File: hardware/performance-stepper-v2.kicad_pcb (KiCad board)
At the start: 4 copper layers, 80 x 80 mm, 111 parts, among them P1 VIN, P101 CON-SENSOR2, P102 DEBUG, P103 BOOT, P2 OUT, P3 GPIO, P4 PROTO, Q1 CSD19533Q5A, Q2 CSD19533Q5A, Q3 CSD19533Q5A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

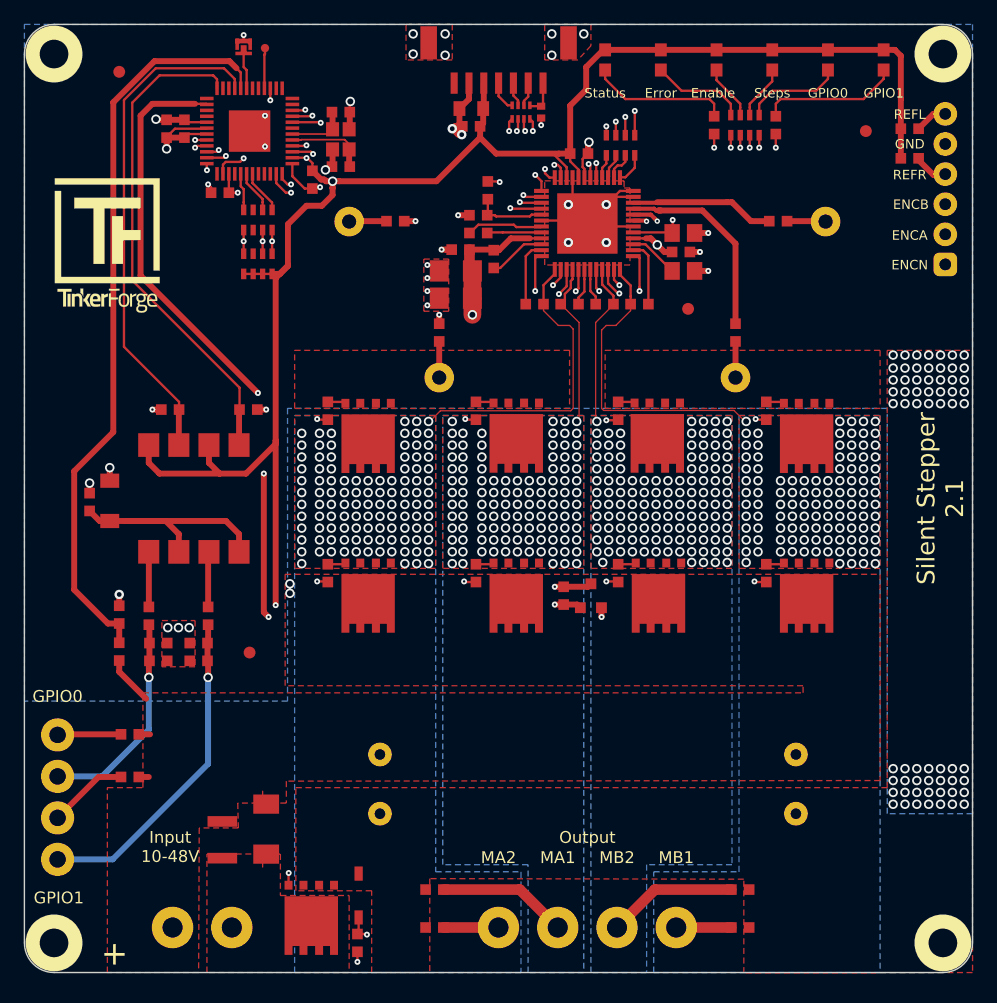
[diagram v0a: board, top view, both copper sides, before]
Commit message: version 2.2 : changed name, added shunt version solderjumpers, moved pins for boot and debug pad, changed silkscreen
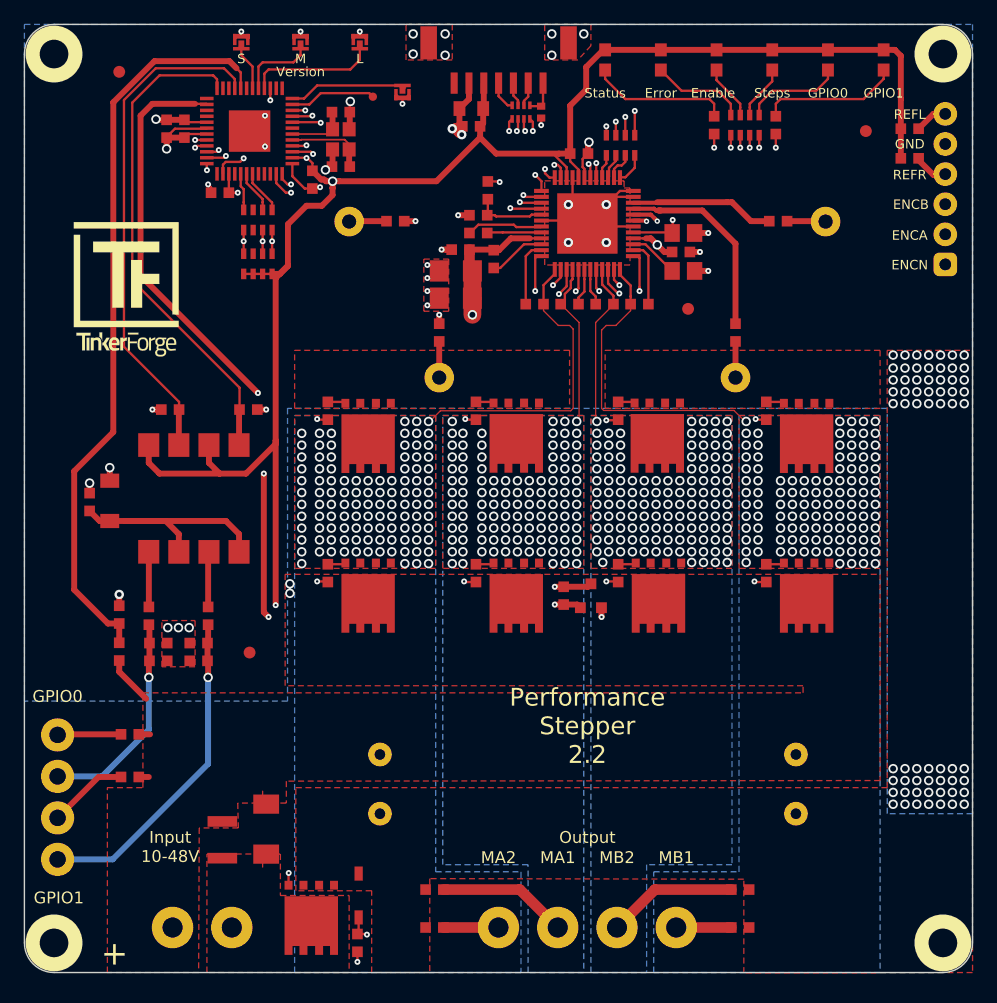
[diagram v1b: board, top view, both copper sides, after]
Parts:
- added P5: L, kicad-libraries:SolderJumper, F.Cu at (73.3, 91.5)
- added P6: M, kicad-libraries:SolderJumper, F.Cu at (68.3, 91.5)
- added P7: S, kicad-libraries:SolderJumper, F.Cu at (63.3, 91.5)
- moved P103 13.9 mm to (76.9, 95.7), turned to 90 degrees
- moved P102 9.98 mm to (74.4, 96.1)
- moved G*** 4.03 mm to (53.6, 112.2)
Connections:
- U2 pad 4: Net-(P102-Pad1) -> Net-(P5-Pad2)
- U2 pad 47: Net-(U2-Pad47) -> Net-(P102-Pad1)
- U2 pad 48: Net-(U2-Pad48) -> Net-(P103-Pad2)
- U2 pad 7: Net-(P103-Pad2) -> Net-(U2-Pad7)
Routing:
- net Net-(P5-Pad2): track 0.00 -> 11.1 mm
- net Net-(P103-Pad2): track 3.44 -> 10.7 mm
- net Net-(P6-Pad2): track 0.00 -> 6.73 mm
- net GND: track 67.3 -> 72.5 mm, vias 104 -> 107
- net Net-(P7-Pad2): track 0.00 -> 4.13 mm
- net Net-(P102-Pad1): track 3.41 -> 7.31 mm
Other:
- board text added: "Copyright Tinkerforge GmbH 2020. This documentation describes Open Hardware and is licensed under the CERN OHL v. 1.1. You may redistribute and modify this documentation under the terms of the CERN OHL v.1.1. (http://ohwr.org/cernohl). This documentation is distributed WITHOUT ANY EXPRESS OR IMPLIED WARRANTY, INCLUDING OF MERCHANTABILITY, SATISFACTORY QUALITY AND FITNESS FOR A PARTICULAR PURPOSE.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"
- board text added: "L"
- board text added: "M"
- board text added: "Performance Stepper 2.2"
- board text added: "S"
- board text added: "Version"
- board text removed: "Silent Stepper 2.1"

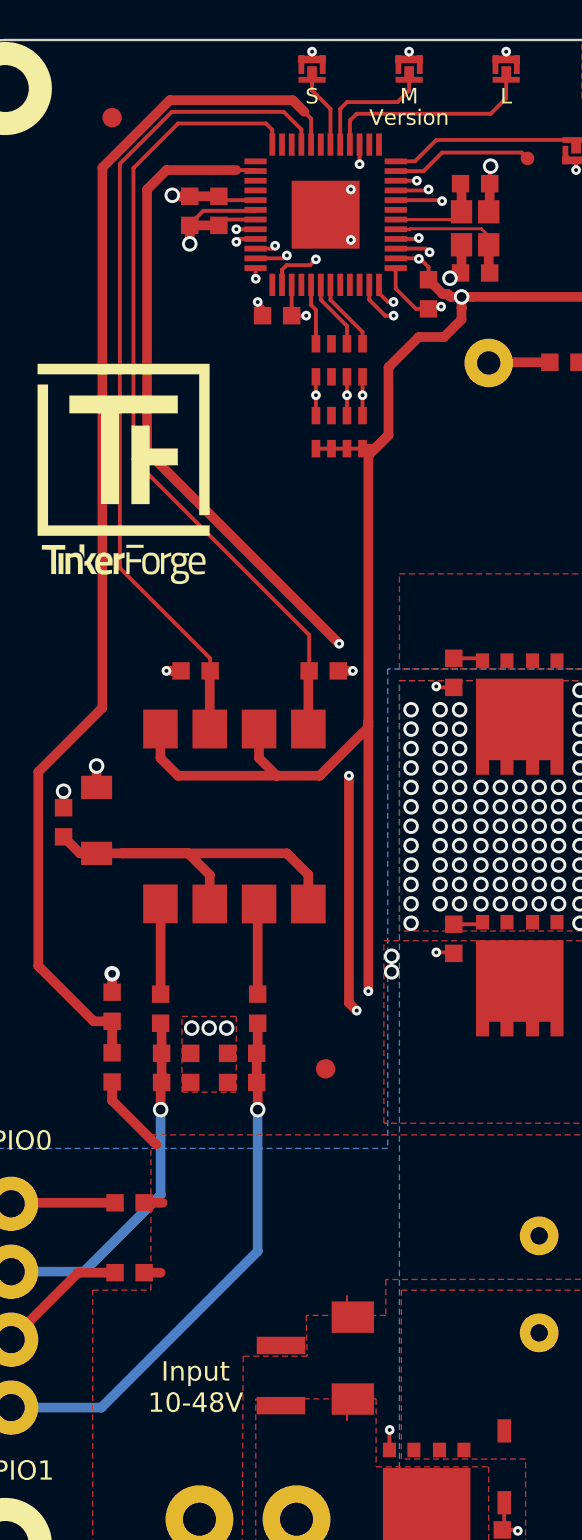
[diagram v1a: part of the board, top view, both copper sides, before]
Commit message: changed silkscreen
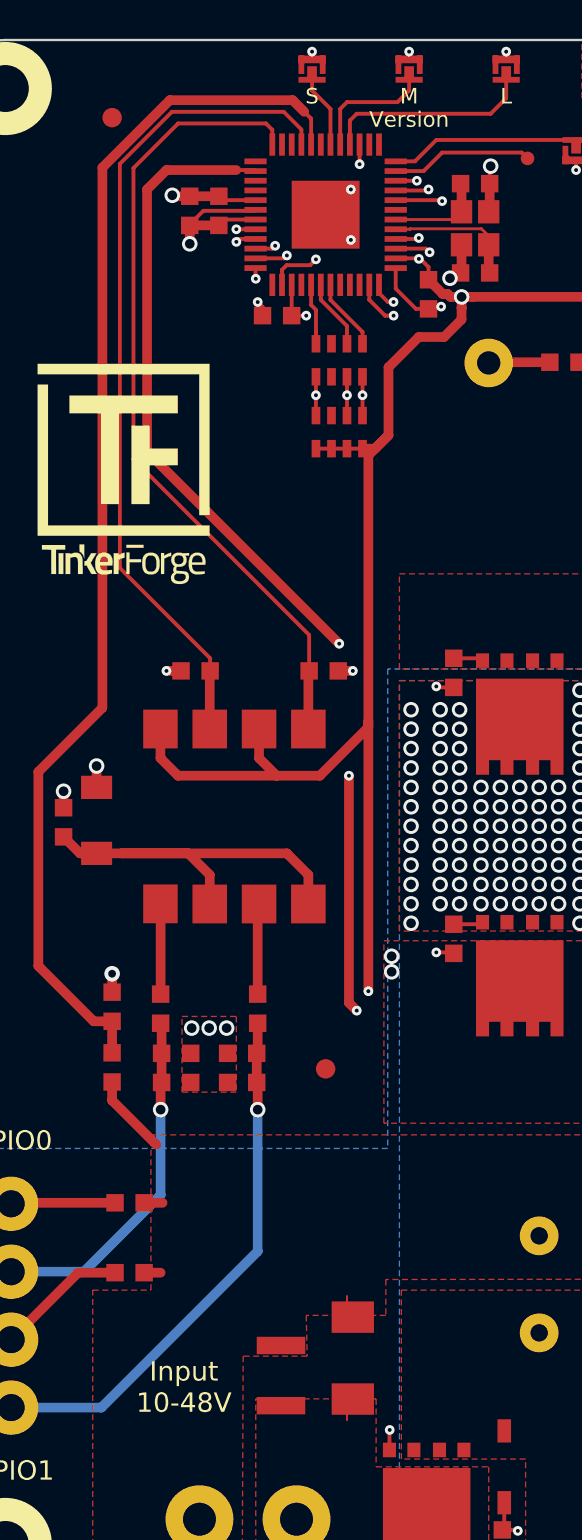
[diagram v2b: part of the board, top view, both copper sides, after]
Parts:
- moved G*** 4.10 mm to (92.5, 150.1)
- moved VAL 4.10 mm to (85.2, 150.5)
- moved VAL 4.10 mm to (100.5, 150.0)
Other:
- board text added: "tinkerforge.com"
